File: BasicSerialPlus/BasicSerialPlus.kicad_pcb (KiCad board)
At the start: 2 copper layers, 129.3 x 124.5 mm, 23 parts, among them CN1 DB9 Male, J1 COM_SELECT, J1 Input BUS, J2 IRQ_SELECT, U1 16550/16C550, U2 74LS688, 74HCT688 or GAL16V8, U3 GD75232N, U4 1.8432 MHz

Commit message: Realized on PLUS cards, the ports need to be on the UNDERSIDE to line up properly
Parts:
- CN1: moved to B.Cu
- turned CN1 to -90 degrees
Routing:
- net /SER_PIN1: track 31.8 -> 19.8 mm, vias 2 -> 0
- net /SER_PIN9: track 34.0 -> 22.1 mm
- net /SER_PIN4: track 26.7 -> 19.1 mm, vias 2 -> 0
- net /SER_PIN6: track 30.1 -> 22.9 mm, vias 2 -> 0
- net /SER_PIN7: track 27.7 -> 21.1 mm
- net /SER_PIN2: track 24.5 -> 18.9 mm, vias 2 -> 0
- net /SER_PIN8: track 22.7 -> 21.1 mm

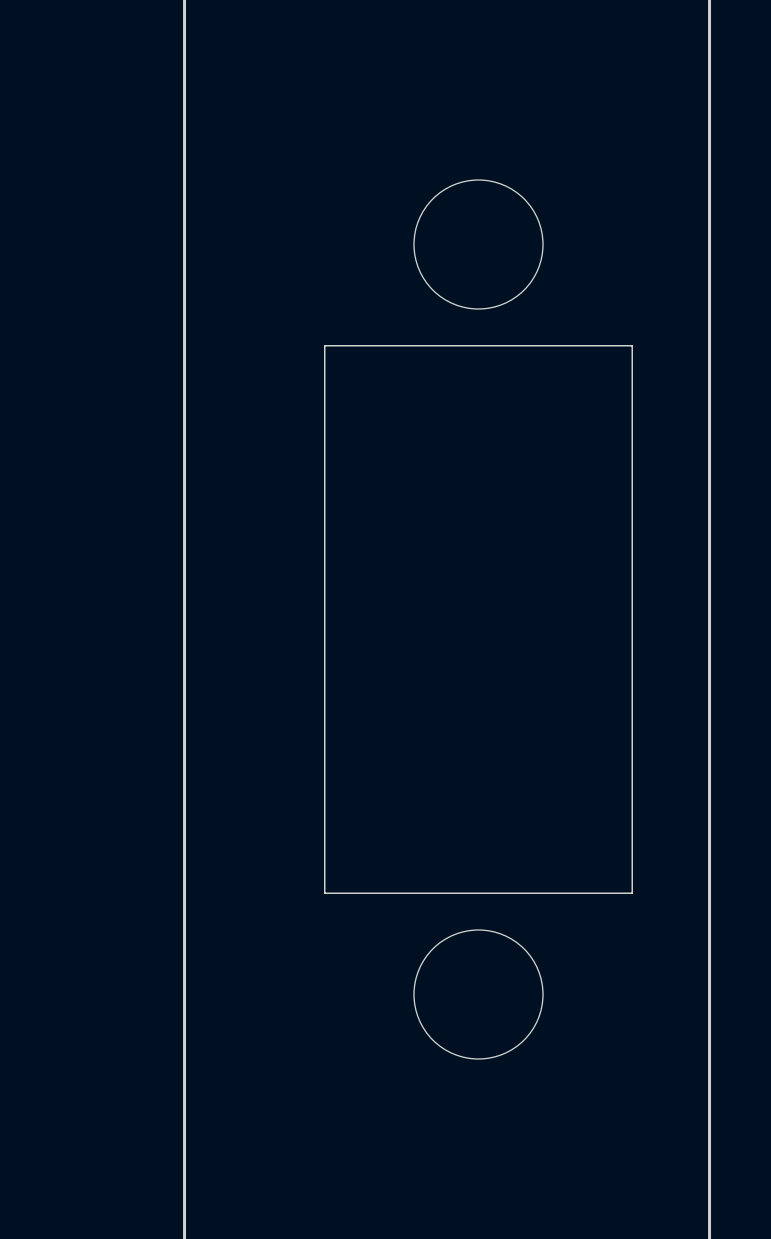
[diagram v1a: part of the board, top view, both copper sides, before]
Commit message: Shifted cutout for basic serial bracket
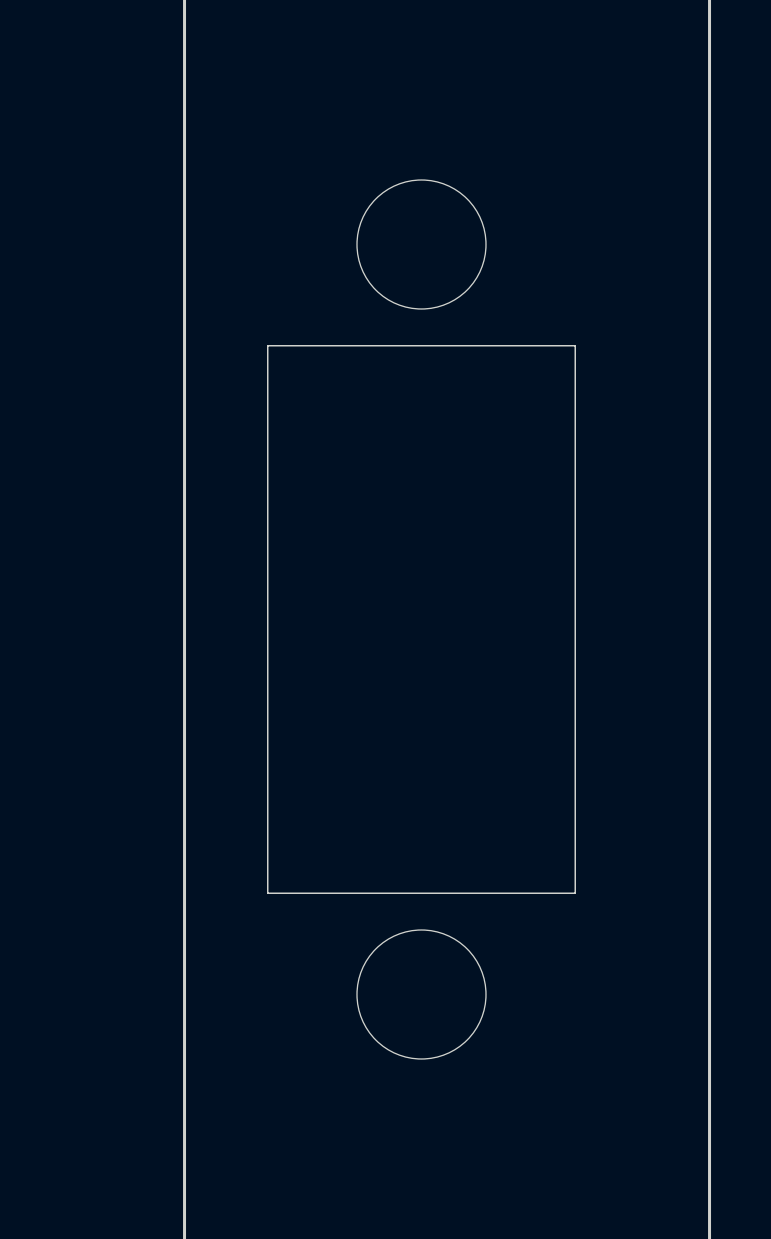
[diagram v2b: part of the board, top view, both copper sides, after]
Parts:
- moved HA1 1.90 mm to (216.3, 61.6)
- moved HA2 1.90 mm to (216.3, 86.6)
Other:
- outline, holes or cut-outs redrawn
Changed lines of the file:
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@@
 	(footprint "MountingHole:MountingHole_4.3mm_M4_DIN965"
 		(layer "F.Cu")
-		(at 218.155 61.62)
+		(at 216.255 61.62)
 		(descr "Mounting Hole 4.3mm, M4, no annular, generated by kicad-footprint-generator mountinghole.py")
 		(tags "mountinghole M4 DIN965")
@@
 	(footprint "MountingHole:MountingHole_4.3mm_M4_DIN965"
 		(layer "F.Cu")
-		(at 218.155 86.62)
+		(at 216.255 86.62)
 		(descr "Mounting Hole 4.3mm, M4, no annular, generated by kicad-footprint-generator mountinghole.py")
 		(tags "mountinghole M4 DIN965")
@@
 	)
 	(gr_rect
-		(start 213.03 64.995)
-		(end 223.28 83.245)
+		(start 211.13 64.995)
+		(end 221.38 83.245)
 		(stroke
 			(width 0.05)
